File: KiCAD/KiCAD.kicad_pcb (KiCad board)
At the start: 2 copper layers, 112.1 x 150 mm, 141 parts, among them J1 Conn_01x02_Pin, J13 Conn_01x05, J15 Conn_01x03_Pin, J16 Conn_01x05, J4 8P8C_Shielded, J5 ENC_INT if needed, J6 TX/RX, J7 HV, J8 HV_INRUSH_BYPASS, J9 TR_SENSE, Q1 J310, Q4 2N7000, Q5 2N7000, Q6 2N7000, Q7 2N7000, T1 2N3906, T2 2N3906, U1 Si5351A_Breakout, U15 LM7805_TO220, U16 AM26LS32ACN, U17 Adafruit_PCF8575_Breakout, U18 CD14538B, U19 L79L08_TO92, U20 ICL7660S, U3 MC1496, U4 MCP4921, U6 LM7171xIN, U7 LM7171xIN, U8 MCP4728

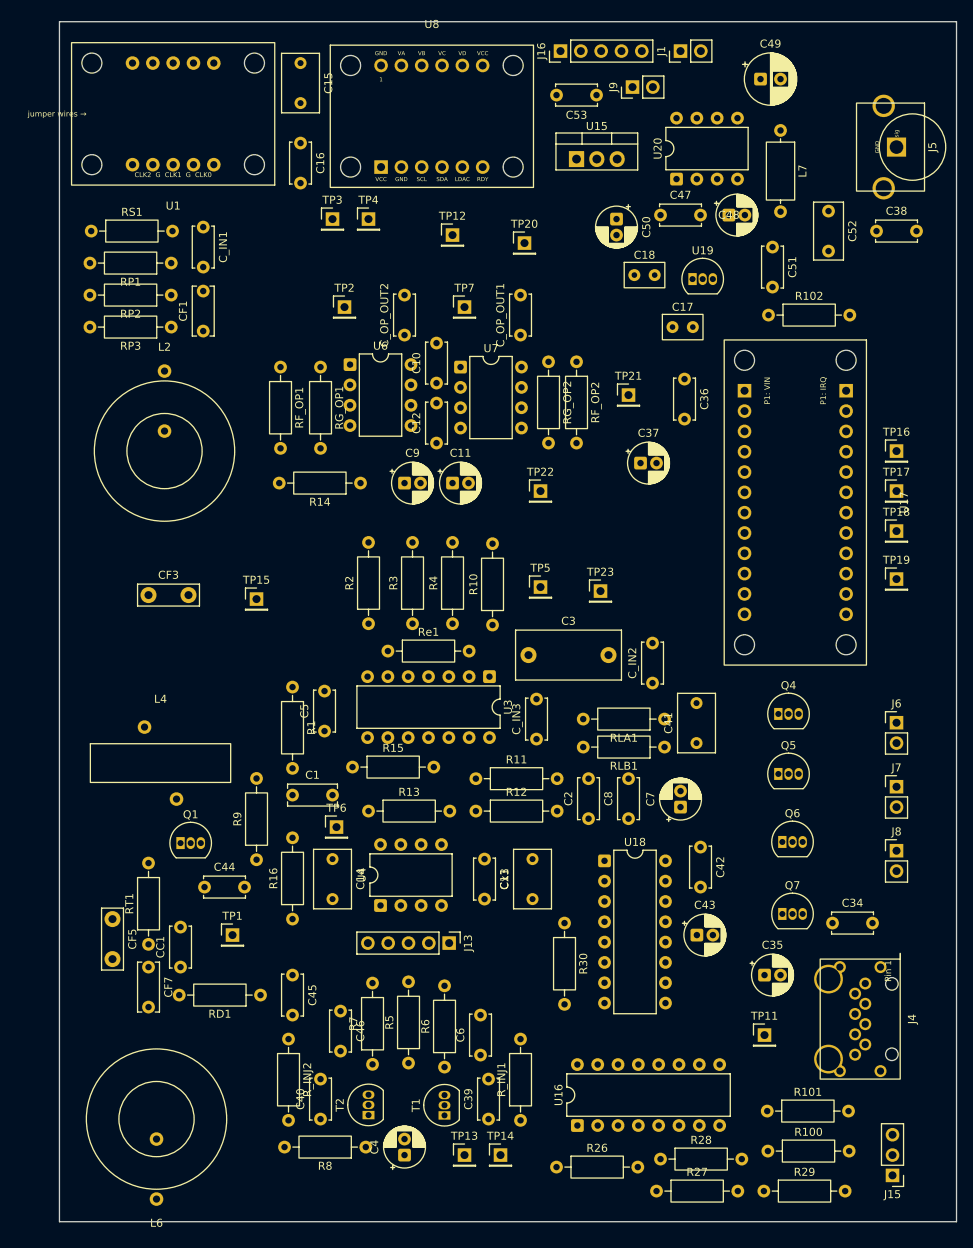
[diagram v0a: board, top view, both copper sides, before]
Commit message: kicad: RJE1D-188 footprint per datasheet + GND zones + net class tweaks
- Rewrite xmitter:Amphenol_RJE1D-188_Horizontal_Shielded to correct
  interpretation from datasheet p-rje1d-188-x1x01.pdf: 8 signal pins in
  staggered rows (front 1,3,5,7 at Y=+3.96; back 2,4,6,8 at Y=+6.50),
  2 Ø1.57 plated shield tails at (+/-7.425, -6.79) tied to GND, 2 Ø3.0
  NPTH plastic locating posts at (+/-5, 0). Origin at post midpoint.
- Add front/back GND zones on F.Cu/B.Cu inside Edge.Cuts
- RF net class clearance 0.25 -> 0.20 to fix Q1 TO-92 DRC clearance error
- Archive datasheet PDF and reference AI-generated footprint under
  Documentation/Components

Co-Authored-By: Claude Opus 4.7 <noreply@anthropic.com>
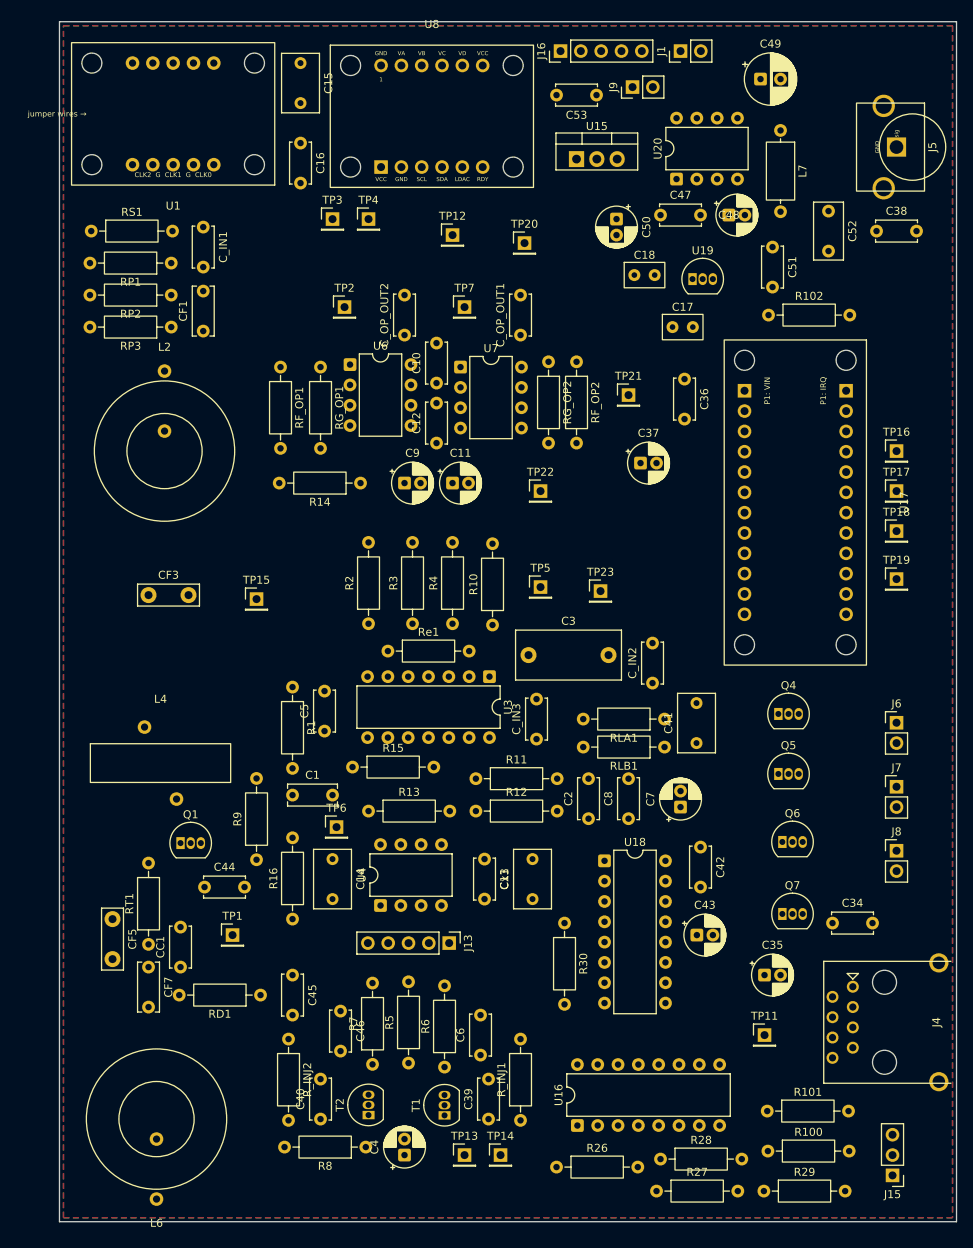
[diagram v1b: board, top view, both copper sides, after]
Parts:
- moved J4 3.07 mm to (119.0, 139.4)
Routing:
- added copper zone on B.Cu, net GND
- added copper zone on F.Cu, net GND
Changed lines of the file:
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@@
 	(footprint "xmitter:Amphenol_RJE1D-188_Horizontal_Shielded"
 		(layer "F.Cu")
-		(at 115.96 139 -90)
-		(descr "Amphenol RJE1D-188-X1X01 shielded RJ45 8P8C jack, right-angle THT, tab-down, no LEDs, no magnetics. Signal pins in staggered 2x4 array (1.27mm x/y offset, 2.54mm in-row pitch, 8.89mm total x-span). Verified from datasheet rev B: 8 signal pins (P1-P8) ø0.90mm; 4 additional shield tail holes ø0.90mm; 2 shield-shell mounting posts ø3.00mm; 2 plastic alignment pegs ø1.57mm. Origin at geometric center of signal pin array. VERIFY EACH SHIELD-TAB AND PEG POSITION AGAINST DATASHEET P2 BEFORE FAB -- extracted from datasheet text, not measured. Signal pin coords are exact.")
-		(tags "amphenol rje1d rj45 8p8c shielded modular jack thru-hole right-angle cat5e")
+		(at 119 139.4 -90)
+		(descr "Amphenol RJE1D18821401 shielded RJ45 8P8C jack, right-angle THT, tab-down, no LEDs, no magnetics. Per user's direct reading of datasheet p-rje1d-188-x1x01.pdf rev B. Layout along Y-axis (opening to back): PCB edge at Y=-8.8; Ø1.57 plated shield tails at Y=-6.79 (14.85mm spacing, GND); Ø3.00 NPTH plastic locating posts at Y=0 (10.00mm spacing, origin datum); front pin row (odd 1,3,5,7) Ø0.9 at Y=+3.96; back pin row (even 2,4,6,8) Ø0.9 at Y=+6.50. Rows staggered by 1.27mm in X. Pin 1 at (-4.445,+3.96), Pin 8 at (+4.445,+6.50). Origin at midpoint between Ø3.00 locating posts.")
+		(tags "amphenol rje1d18821401 rj45 8p8c shielded modular jack thru-hole right-angle cat5e")
 		(property "Reference" "J4"
 			(at 0 -6.5 90)
@@
 		(duplicate_pad_numbers_are_jumpers no)
 		(fp_line
-			(start -7.5 -5)
-			(end -8.2 -5)
+			(start -7.62 7.6)
+			(end 7.62 7.6)
 			(stroke
-				(width 0.2)
+				(width 0.12)
 				(type solid)
 			)
 			(layer "F.SilkS")
 		)
-		(fp_rect
-			(start -7.5 -5)
-			(end 7.5 5)
+		(fp_line
+			(start -6.1 4.66)
+			(end -5.4 3.96)
+			(stroke
+				(width 0.15)
+				(type solid)
+			)
+			(layer "F.SilkS")
+		)
+		(fp_line
+			(start -5.4 3.96)
+			(end -6.1 3.26)
+			(stroke
+				(width 0.15)
+				(type solid)
+			)
+			(layer "F.SilkS")
+		)
+		(fp_line
+			(start -6.1 3.26)
+			(end -6.1 4.66)
+			(stroke
+				(width 0.15)
+				(type solid)
+			)
+			(layer "F.SilkS")
+		)
+		(fp_line
+			(start -7.62 -8.3)
+			(end -7.62 7.6)
+			(stroke
+				(width 0.12)
+				(type solid)
+			)
+			(layer "F.SilkS")
+		)
+		(fp_line
+			(start 7.62 -8.3)
+			(end 7.62 7.6)
 			(stroke
 				(width 0.12)
 				(type solid)
 			)
-			(fill no)
 			(layer "F.SilkS")
 		)
+		(fp_line
+			(start -9 -8.8)
+			(end 9 -8.8)
+			(stroke
+				(width 0.15)
+				(type dash)
+			)
+			(layer "Dwgs.User")
+		)
 		(fp_rect
-			(start -8.5 -6)
-			(end 8.5 6)
+			(start -8 -9.3)
+			(end 8 8.1)
 			(stroke
 				(width 0.05)
@@
 		)
 		(fp_rect
-			(start -7.5 -5)
-			(end 7.5 5)
+			(start -7.5 -13.3)
+			(end 7.5 7.58)
 			(stroke
 				(width 0.1)
@@
 		(fp_text user "Pin 1"
 			(at -6 -3.5 90)
-			(layer "F.SilkS")
+			(layer "Dwgs.User")
 			(effects
 				(font
@@
 		)
 		(pad "" np_thru_hole circle
-			(at -4.4 -3.96 270)
-			(size 1.57 1.57)
-			(drill 1.57)
+			(at -5 0 270)
+			(size 3 3)
+			(drill 3)
 			(layers "*.Cu" "*.Mask")
 		)
 		(pad "" np_thru_hole circle
-			(at 4.4 -3.96 270)
-			(size 1.57 1.57)
-			(drill 1.57)
+			(at 5 0 270)
+			(size 3 3)
+			(drill 3)
 			(layers "*.Cu" "*.Mask")
 		)
 		(pad "1" thru_hole circle
-			(at -4.445 -0.635 270)
+			(at -4.445 3.96 270)
 			(size 1.5 1.5)
 			(drill 0.9)
@@
 		)
 		(pad "2" thru_hole circle
-			(at -3.175 0.635 270)
+			(at -3.175 6.5 270)
 			(size 1.5 1.5)
 			(drill 0.9)
@@
 		)
 		(pad "3" thru_hole circle
-			(at -1.905 -0.635 270)
+			(at -1.905 3.96 270)
 			(size 1.5 1.5)
 			(drill 0.9)
@@
 		)
 		(pad "4" thru_hole circle
-			(at -0.635 0.635 270)
+			(at -0.635 6.5 270)
 			(size 1.5 1.5)
 			(drill 0.9)
@@
 		)
 		(pad "5" thru_hole circle
-			(at 0.635 -0.635 270)
+			(at 0.635 3.96 270)
 			(size 1.5 1.5)
 			(drill 0.9)
@@
 		)
 		(pad "6" thru_hole circle
-			(at 1.905 0.635 270)
+			(at 1.905 6.5 270)
 			(size 1.5 1.5)
 			(drill 0.9)
@@
 		)
 		(pad "7" thru_hole circle
-			(at 3.175 -0.635 270)
+			(at 3.175 3.96 270)
 			(size 1.5 1.5)
 			(drill 0.9)
@@
 		)
 		(pad "8" thru_hole circle
-			(at 4.445 0.635 270)
+			(at 4.445 6.5 270)
 			(size 1.5 1.5)
 			(drill 0.9)
@@
 		)
 		(pad "SH" thru_hole circle
-			(at -6.5 -2.54 270)
-			(size 1.5 1.5)
-			(drill 0.9)
-			(layers "*.Cu" "*.Mask")
-			(remove_unused_layers no)
-			(net "GND")
-			(pintype "passive")
-		)
-		(pad "SH" thru_hole circle
-			(at -6.5 2.54 270)
-			(size 1.5 1.5)
-			(drill 0.9)
-			(layers "*.Cu" "*.Mask")
-			(remove_unused_layers no)
-			(net "GND")
-			(pintype "passive")
-		)
-		(pad "SH" thru_hole circle
-			(at -5 3.96 270)
-			(size 3.6 3.6)
-			(drill 3)
-			(layers "*.Cu" "*.Mask")
-			(remove_unused_layers no)
-			(net "GND")
-			(pintype "passive")
-		)
-		(pad "SH" thru_hole circle
-			(at 5 3.96 270)
-			(size 3.6 3.6)
-			(drill 3)
-			(layers "*.Cu" "*.Mask")
-			(remove_unused_layers no)
-			(net "GND")
-			(pintype "passive")
-		)
-		(pad "SH" thru_hole circle
-			(at 6.5 -2.54 270)
-			(size 1.5 1.5)
-			(drill 0.9)
+			(at -7.425 -6.79 270)
+			(size 2.4 2.4)
+			(drill 1.57)
 			(layers "*.Cu" "*.Mask")
 			(remove_unused_layers no)
@@
 		)
 		(pad "SH" thru_hole circle
-			(at 6.5 2.54 270)
-			(size 1.5 1.5)
-			(drill 0.9)
+			(at 7.425 -6.79 270)
+			(size 2.4 2.4)
+			(drill 1.57)
 			(layers "*.Cu" "*.Mask")
 			(remove_unused_layers no)
@@
 		(layer "Edge.Cuts")
 	)
+	(zone
+		(net "GND")
+		(layer "F.Cu")
+		(hatch edge 0.5)
+		(connect_pads
+			(clearance 0.2)
+		)
+		(min_thickness 0.25)
+		(fill yes
+			(thermal_gap 0.5)
+			(thermal_bridge_width 0.5)
+			(island_removal_mode 0)
+		)
+		(polygon
+			(pts
+				(xy 16.37 14.83) (xy 127.5 14.83) (xy 127.5 163.83) (xy 16.37 163.83)
+			)
+		)
+	)
+	(zone
+		(net "GND")
+		(layer "B.Cu")
+		(hatch edge 0.5)
+		(connect_pads
+			(clearance 0.2)
+		)
+		(min_thickness 0.25)
+		(fill yes
+			(thermal_gap 0.5)
+			(thermal_bridge_width 0.5)
+			(island_removal_mode 0)
+		)
+		(polygon
+			(pts
+				(xy 16.37 14.83) (xy 127.5 14.83) (xy 127.5 163.83) (xy 16.37 163.83)
+			)
+		)
+	)
 	(embedded_fonts no)

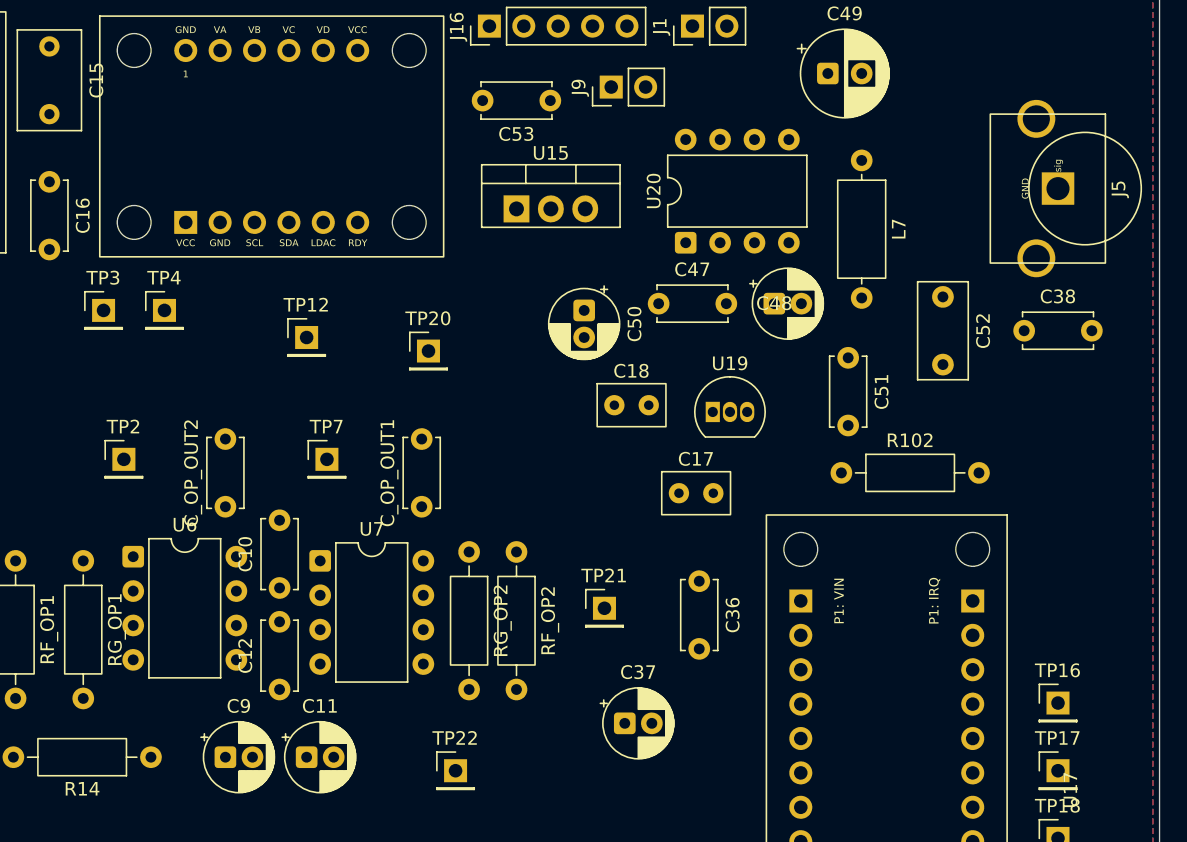
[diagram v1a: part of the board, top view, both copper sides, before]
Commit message: kicad: initial routing, netclass tweaks, routing cheatsheet
- Start routing on buffer_keyer PCB (VEE + Net-(U19-VI))
- Netclass assignments and pattern updates for anonymous power nets
  (U19/U20 chain)
- Schematic tweaks alongside routing pass
- Add Documentation/kicad_routing_cheatsheet.md — box-drawing tables
  for shortcut reference readable in `less`

Co-Authored-By: Claude Opus 4.7 <noreply@anthropic.com>
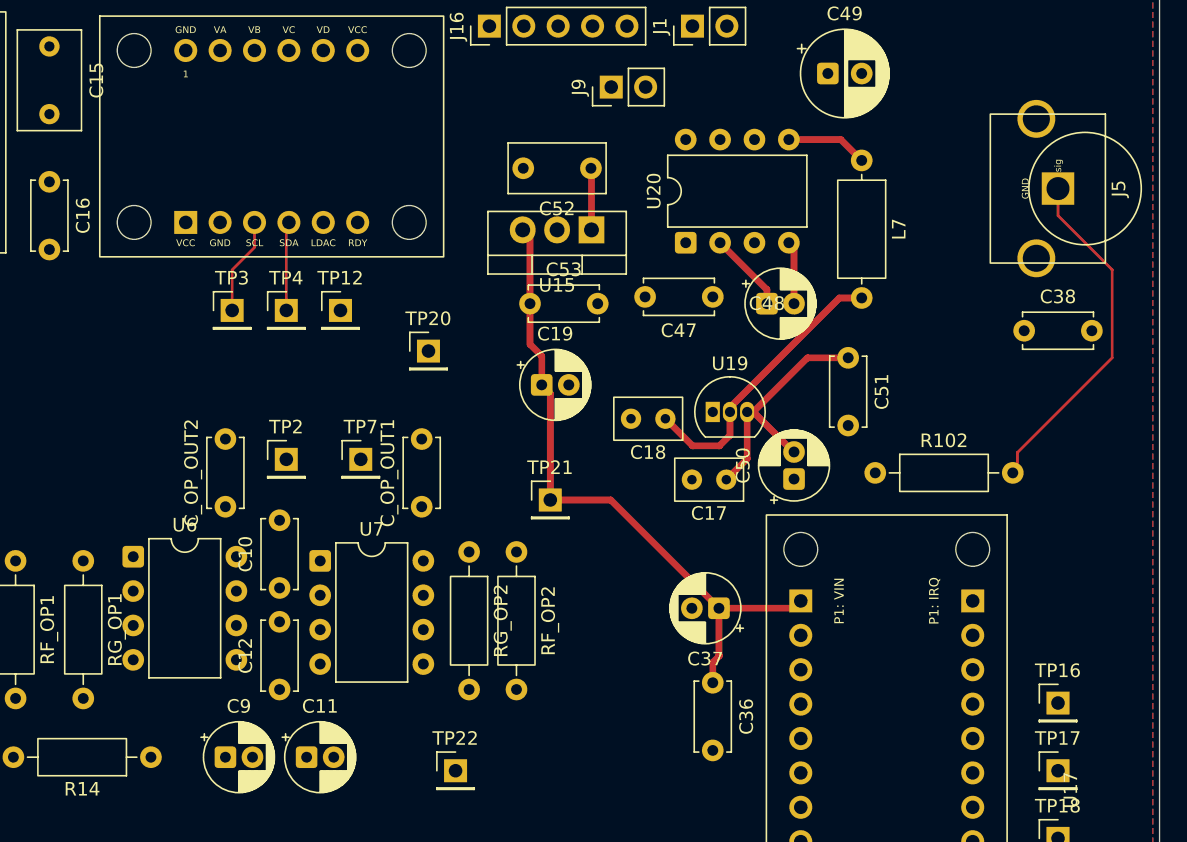
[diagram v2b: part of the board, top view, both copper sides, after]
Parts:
- added C19: 10uF, Capacitor_THT:CP_Radial_D5.0mm_P2.00mm, F.Cu at (82.4, 44.5)
- moved C52 27.7 mm to (86.0, 28.5), turned to 180 degrees
- moved C50 19.9 mm to (101.0, 51.5), turned to 90 degrees
- moved C53 15.1 mm to (81.5, 38.5), turned to 0 degrees
- moved TP2 12.0 mm to (63.5, 50.0)
- moved C37 11.0 mm to (95.5, 61.0), turned to 180 degrees
- moved TP3 9.50 mm to (59.5, 39.0)
- moved TP4 9.00 mm to (63.5, 39.0)
- moved TP21 8.94 mm to (83.0, 53.0)
- moved C36 7.57 mm to (95.0, 66.5)
- moved U15 5.75 mm to (86.0, 33.0), turned to 180 degrees
- moved C47 4.03 mm to (95.0, 38.0), turned to 180 degrees
- moved TP12 3.20 mm to (67.5, 39.0)
- moved R102 2.50 mm to (107.0, 51.0)
- moved TP7 2.50 mm to (69.0, 50.0)
- moved C18 1.59 mm to (90.2, 47.0), turned to 180 degrees
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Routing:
- net +5V: track 0.00 -> 48.7 mm
- net Net-(J5-In): track 0.00 -> 25.7 mm
- net Net-(U19-VI): track 0.00 -> 21.1 mm
- net VEE: track 0.00 -> 19.1 mm
- net SCL: track 0.00 -> 7.18 mm
- net SDA: track 0.00 -> 6.58 mm
- net Net-(U20-VOUT): track 0.00 -> 6.02 mm
- net Net-(U20-CAP+): track 0.00 -> 5.93 mm
- net Net-(U20-CAP-): track 0.00 -> 4.66 mm
- net +12V: track 0.00 -> 4.57 mm
